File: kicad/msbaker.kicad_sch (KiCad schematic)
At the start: 38 parts, among them J1 USB_B_Micro, J2 Micro_SD_Card, J3 GPIO, U1 MIC5365-3.3YC5, U2 W25Q128JVS, U3 RP2040, U4 LSM6DSO32, Y1 12MHz

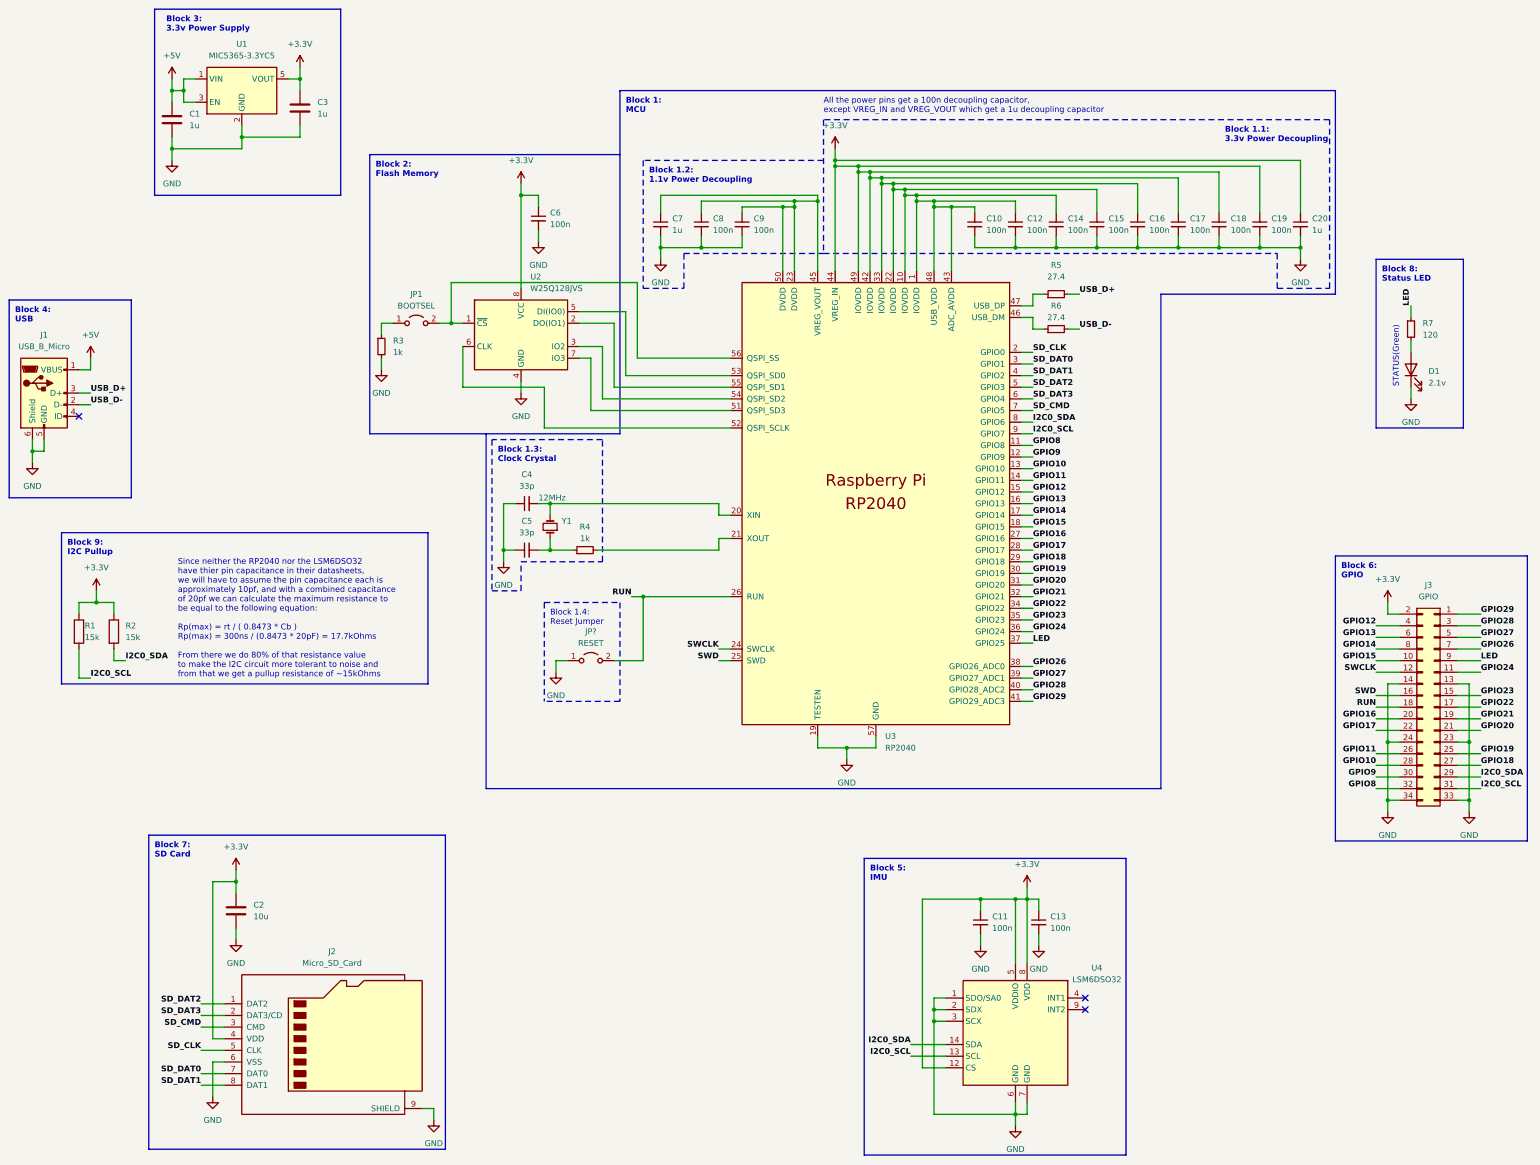
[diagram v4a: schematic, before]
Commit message: Separated the bootsel jumper into it's own block
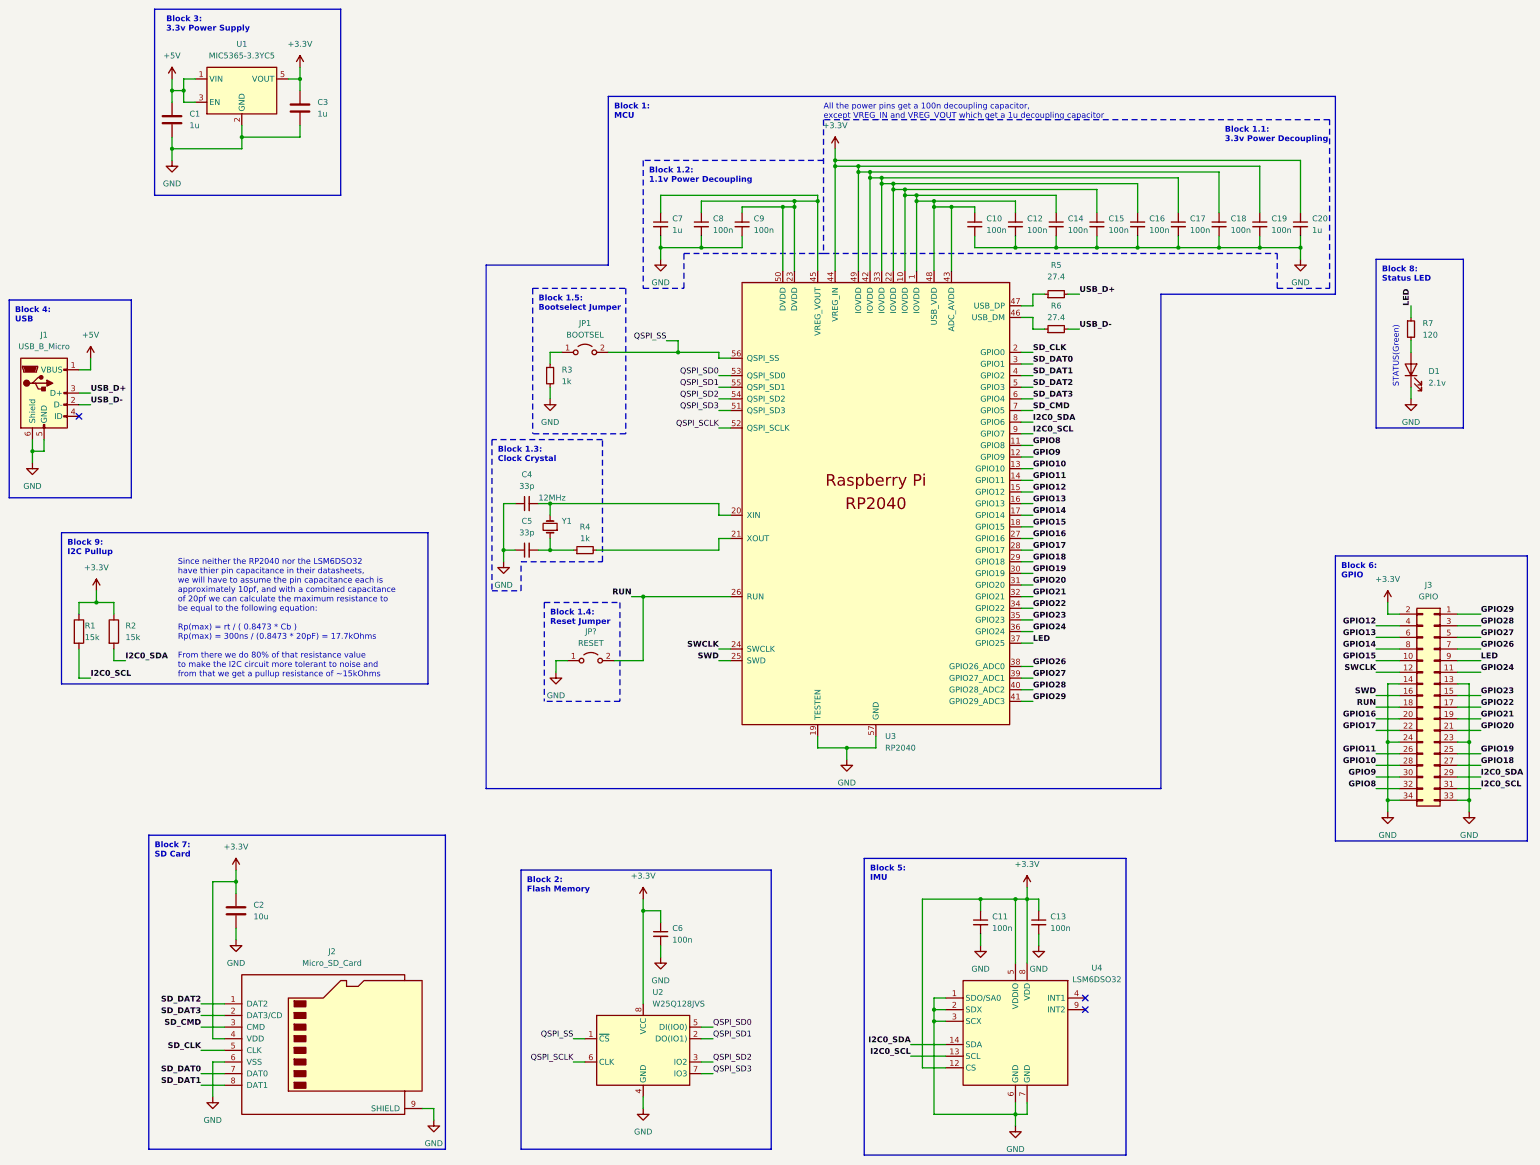
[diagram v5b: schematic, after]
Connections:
- net QSPI_SS: now reaches JP1.2 (B), U2.1 (~{CS}), U3.56 (QSPI_SS)
- net QSPI_SD1: now reaches U2.2 (DO(IO1)), U3.55 (QSPI_SD1)
- net QSPI_SD2: now reaches U2.3 (IO2), U3.54 (QSPI_SD2)
- net QSPI_SD0: now reaches U2.5 (DI(IO0)), U3.53 (QSPI_SD0)
- net QSPI_SCLK: now reaches U2.6 (CLK), U3.52 (QSPI_SCLK)
- net QSPI_SD3: now reaches U2.7 (IO3), U3.51 (QSPI_SD3)
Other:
- note added: "Block 1.5: Bootselect Jumper"
- moved on the sheet: C6, JP1, R3, U2
